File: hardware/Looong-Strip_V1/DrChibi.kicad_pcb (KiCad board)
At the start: 4 copper layers, 143.5 x 14 mm, 284 parts, among them P1 CONN_02X05, P3 IN+, P4 IN-, P5 CONN_01X04, U1 STM32F40X_LQFP64, U2 ISO1050, X1 MINI-USB-SHIELD-32005-201, X2 8MHz 10ppm

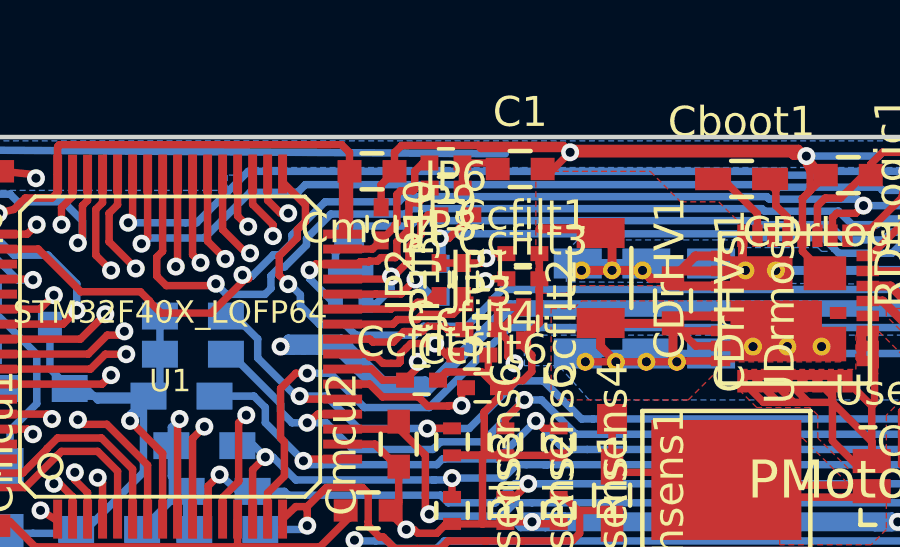
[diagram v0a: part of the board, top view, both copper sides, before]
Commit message: Fixed little DRC problem.
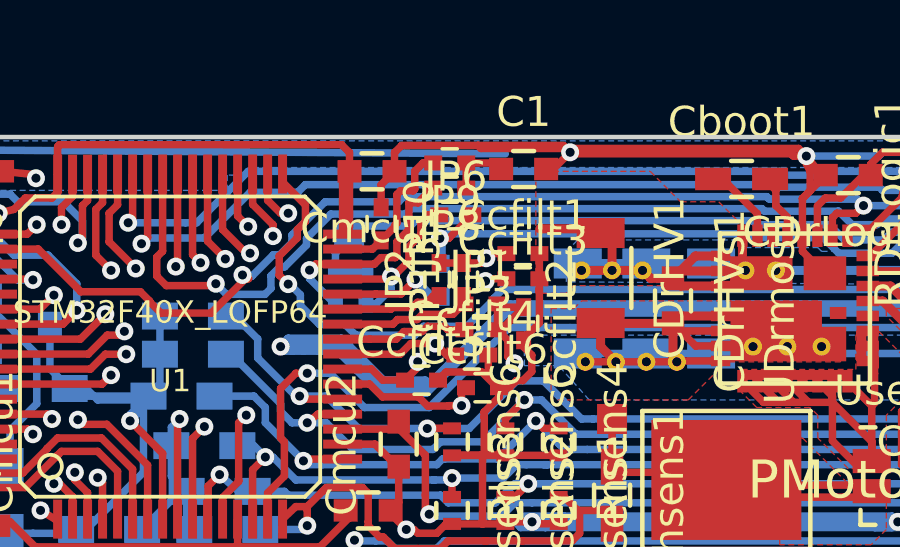
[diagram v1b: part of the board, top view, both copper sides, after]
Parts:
- moved JP9 0.13 mm to (82.6, 93.9)
- moved JP8 0.12 mm to (82.6, 94.7)
- moved C1 0.12 mm to (85.1, 94.1)
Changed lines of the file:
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@@
     (thickness 1.6)
     (drawings 44)
-    (tracks 3797)
+    (tracks 3783)
     (zones 0)
     (modules 284)
@@
   (layers
     (0 F.Cu signal)
-    (1 In1.Cu mixed)
-    (2 In2.Cu mixed)
-    (31 B.Cu signal)
+    (1 In1.Cu mixed hide)
+    (2 In2.Cu mixed hide)
+    (31 B.Cu signal hide)
     (33 F.Adhes user)
     (34 B.Paste user)
@@
     (41 Cmts.User user)
     (42 Eco1.User user)
-    (43 Eco2.User user)
-    (44 Edge.Cuts user)
+    (43 Eco2.User user hide)
+    (44 Edge.Cuts user hide)
     (45 Margin user)
     (47 F.CrtYd user)
     (48 B.Fab user)
-    (49 F.Fab user)
+    (49 F.Fab user hide)
   )
   (setup
@@
     (aux_axis_origin 54.75 130.48)
     (grid_origin 54.75 130.48)
-    (visible_elements FFFCFF7F)
+    (visible_elements FFFC7F7F)
     (pcbplotparams
       (layerselection 0x310dc_ffffffff)
@@
   )
   (module Capacitors_SMD:C_0603 (layer F.Cu)
-    (at 84.9626 94.0818)
+    (at 85.0776 94.0818)
     (descr "Capacitor SMD 0603, reflow soldering, AVX (see smccp.pdf)")
     (tags "capacitor 0603")
@@
   )
   (module Capacitors_SMD:C_0402 (layer F.Cu)
-    (at 82.4956 94.7168 180)
+    (at 82.6138 94.7168 180)
     (descr "Capacitor SMD 0402, reflow soldering, AVX (see smccp.pdf)")
     (tags "capacitor 0402")
@@
   )
   (module Capacitors_SMD:C_0402 (layer F.Cu)
-    (at 82.4868 93.8786 180)
+    (at 82.6138 93.8786 180)
     (descr "Capacitor SMD 0402, reflow soldering, AVX (see smccp.pdf)")
     (tags "capacitor 0402")
@@
   (segment (start 137.935 95.301) (end 138.193 95.559) (width 0.25) (layer F.Cu) (net 52))
   (segment (start 138.193 95.559) (end 138.193 96.305) (width 0.25) (layer F.Cu) (net 52))
+  (segment (start 79.04256 100.24892) (end 79.40832 100.24892) (width 0.25) (layer F.Cu) (net 53))
+  (segment (start 79.40832 100.24892) (end 79.4134 100.254) (width 0.25) (layer F.Cu) (net 53))
+  (segment (start 79.4134 100.254) (end 80.9628 100.254) (width 0.25) (layer F.Cu) (net 53))
+  (segment (start 80.9628 100.254) (end 81.3184 99.8984) (width 0.25) (layer F.Cu) (net 53))
+  (segment (start 81.3184 99.8984) (end 82.1312 99.8984) (width 0.25) (layer F.Cu) (net 53))
   (segment (start 82.8004 100.2794) (end 82.563 100.2794) (width 0.25) (layer F.Cu) (net 53))
   (segment (start 82.563 100.2794) (end 82.5376 100.3048) (width 0.25) (layer F.Cu) (net 53))
-  (segment (start 80.658 100.5588) (end 80.912 100.5588) (width 0.25) (layer F.Cu) (net 53))
-  (segment (start 82.1312 99.8984) (end 81.3184 99.8984) (width 0.25) (layer F.Cu) (net 53))
-  (segment (start 81.166 100.0508) (end 81.3184 99.8984) (width 0.25) (layer F.Cu) (net 53))
-  (segment (start 80.658 100.5588) (end 80.4548 100.5588) (width 0.25) (layer F.Cu) (net 53))
-  (segment (start 80.383318 100.5588) (end 80.173808 100.34929) (width 0.25) (layer F.Cu) (net 53))
-  (segment (start 80.4548 100.5588) (end 80.383318 100.5588) (width 0.25) (layer F.Cu) (net 53))
-  (segment (start 80.173808 100.34929) (end 79.9468 100.34929) (width 0.25) (layer F.Cu) (net 53))
-  (segment (start 80.9628 100.254) (end 81.166 100.0508) (width 0.25) (layer F.Cu) (net 53))
-  (segment (start 80.9628 100.508) (end 80.9628 100.254) (width 0.25) (layer F.Cu) (net 53))
-  (segment (start 80.912 100.5588) (end 80.9628 100.508) (width 0.25) (layer F.Cu) (net 53))
-  (segment (start 79.04256 100.24892) (end 79.846422 100.24892) (width 0.25) (layer F.Cu) (net 53))
-  (segment (start 79.846422 100.24892) (end 79.9468 100.349298) (width 0.25) (layer F.Cu) (net 53))
-  (segment (start 79.9468 100.349298) (end 79.9468 100.34929) (width 0.25) (layer F.Cu) (net 53))
-  (segment (start 79.9468 100.34929) (end 79.9468 100.34929) (width 0.25) (layer F.Cu) (net 53))
   (segment (start 82.5376 100.3048) (end 82.1312 99.8984) (width 0.25) (layer F.Cu) (net 53))
   (via (at 82.1312 99.8984) (size 0.6) (drill 0.3) (layers F.Cu B.Cu) (net 53))
@@
   (segment (start 72.954 101.27) (end 72.573 101.651) (width 0.25) (layer B.Cu) (net 63))
   (segment (start 72.954 98.984) (end 72.954 100.254) (width 0.25) (layer B.Cu) (net 63))
-  (segment (start 83.0368 93.8786) (end 83.0368 94.708) (width 0.25) (layer F.Cu) (net 64))
+  (segment (start 83.1638 93.8786) (end 83.1638 94.7168) (width 0.25) (layer F.Cu) (net 64))
   (segment (start 83.0368 94.708) (end 83.0456 94.7168) (width 0.25) (layer F.Cu) (net 64))
   (segment (start 83.0368 93.8786) (end 84.0094 93.8786) (width 0.25) (layer F.Cu) (net 64))
@@
   (segment (start 82.5552 99.4412) (end 82.437399 99.323399) (width 0.25) (layer F.Cu) (net 108))
   (segment (start 82.437399 99.323399) (end 81.868001 99.323399) (width 0.25) (layer F.Cu) (net 108))
-  (segment (start 80.7342 99.8476) (end 80.0484 99.8476) (width 0.25) (layer F.Cu) (net 108))
   (segment (start 81.868001 99.323399) (end 81.69301 99.49839) (width 0.25) (layer F.Cu) (net 108))
   (segment (start 81.69301 99.49839) (end 81.08341 99.49839) (width 0.25) (layer F.Cu) (net 108))
-  (segment (start 81.08341 99.49839) (end 80.7342 99.8476) (width 0.25) (layer F.Cu) (net 108))
-  (segment (start 80.0484 99.8476) (end 79.95188 99.75108) (width 0.25) (layer F.Cu) (net 108))
+  (segment (start 80.83072 99.75108) (end 79.95188 99.75108) (width 0.25) (layer F.Cu) (net 108))
+  (segment (start 81.08341 99.49839) (end 80.83072 99.75108) (width 0.25) (layer F.Cu) (net 108))
   (segment (start 79.95188 99.75108) (end 79.04256 99.75108) (width 0.25) (layer F.Cu) (net 108))
   (segment (start 80.6326 98.1028) (end 80.642664 98.1028) (width 0.25) (layer B.Cu) (net 109))
@@
   (segment (start 80.14492 98.2474) (end 80.9882 98.2474) (width 0.25) (layer F.Cu) (net 110))
   (segment (start 80.14746 98.24994) (end 80.14492 98.2474) (width 0.25) (layer F.Cu) (net 110))
+  (segment (start 79.04256 97.24918) (end 80.104919 97.24918) (width 0.25) (layer F.Cu) (net 111))
+  (segment (start 81.55869 95.208011) (end 81.674 95.092701) (width 0.25) (layer F.Cu) (net 111))
+  (segment (start 81.258989 95.208011) (end 81.55869 95.208011) (width 0.25) (layer F.Cu) (net 111))
+  (segment (start 81.252811 95.214189) (end 81.258989 95.208011) (width 0.25) (layer F.Cu) (net 111))
+  (segment (start 81.252811 96.101287) (end 81.252811 95.214189) (width 0.25) (layer F.Cu) (net 111))
+  (segment (start 80.852801 96.501297) (end 81.252811 96.101287) (width 0.25) (layer F.Cu) (net 111))
+  (segment (start 80.318498 97.035601) (end 80.797801 97.035601) (width 0.25) (layer F.Cu) (net 111))
+  (segment (start 80.852801 96.980601) (end 80.852801 96.501297) (width 0.25) (layer F.Cu) (net 111))
+  (segment (start 80.797801 97.035601) (end 80.852801 96.980601) (width 0.25) (layer F.Cu) (net 111))
+  (segment (start 80.104919 97.24918) (end 80.318498 97.035601) (width 0.25) (layer F.Cu) (net 111))
   (segment (start 78.8038 98.5942) (end 77.9402 97.7306) (width 0.25) (layer B.Cu) (net 111))
   (segment (start 77.9402 97.7306) (end 77.9402 97.4513) (width 0.25) (layer B.Cu) (net 111))
@@
   (segment (start 79.04256 97.24918) (end 78.14232 97.24918) (width 0.25) (layer F.Cu) (net 111))
   (segment (start 78.14232 97.24918) (end 77.9402 97.4513) (width 0.25) (layer F.Cu) (net 111))
-  (segment (start 81.55869 95.208011) (end 81.674 95.092701) (width 0.25) (layer F.Cu) (net 111))
   (segment (start 81.674 95.092701) (end 81.848011 94.91869) (width 0.25) (layer F.Cu) (net 111))
   (segment (start 81.9456 94.7168) (end 81.9456 94.821101) (width 0.25) (layer F.Cu) (net 111))
   (segment (start 81.9456 94.821101) (end 81.674 95.092701) (width 0.25) (layer F.Cu) (net 111))
-  (segment (start 79.04256 97.24918) (end 79.54802 97.24918) (width 0.25) (layer F.Cu) (net 111))
-  (segment (start 80.852801 96.980601) (end 80.852801 96.501297) (width 0.25) (layer F.Cu) (net 111))
-  (segment (start 79.623399 97.173801) (end 79.912801 97.173801) (width 0.25) (layer F.Cu) (net 111))
-  (segment (start 79.54802 97.24918) (end 79.623399 97.173801) (width 0.25) (layer F.Cu) (net 111))
-  (segment (start 81.252811 96.101287) (end 81.252811 95.214189) (width 0.25) (layer F.Cu) (net 111))
-  (segment (start 79.912801 97.173801) (end 79.937792 97.14881) (width 0.25) (layer F.Cu) (net 111))
-  (segment (start 79.937792 97.14881) (end 80.205289 97.14881) (width 0.25) (layer F.Cu) (net 111))
-  (segment (start 80.205289 97.14881) (end 80.318498 97.035601) (width 0.25) (layer F.Cu) (net 111))
-  (segment (start 80.318498 97.035601) (end 80.797801 97.035601) (width 0.25) (layer F.Cu) (net 111))
-  (segment (start 80.797801 97.035601) (end 80.852801 96.980601) (width 0.25) (layer F.Cu) (net 111))
-  (segment (start 80.852801 96.501297) (end 81.252811 96.101287) (width 0.25) (layer F.Cu) (net 111))
-  (segment (start 81.252811 95.214189) (end 81.258989 95.208011) (width 0.25) (layer F.Cu) (net 111))
-  (segment (start 81.258989 95.208011) (end 81.55869 95.208011) (width 0.25) (layer F.Cu) (net 111))
   (zone (net 2) (net_name GND) (layer In1.Cu) (hatch edge 0.508)
     (connect_pads yes (clearance 0.308))
